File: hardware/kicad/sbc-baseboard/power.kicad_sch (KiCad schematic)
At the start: 85 parts, among them J17 Qwiic PD programming, J2 USB-C PD in, Q101 2N7002, Q102 2N7002, U101 STUSB4500QTR, U102 PCA9517A, U103 TPS54560BDDA, U104 TPS54560BDDA, U105 TPS62823DLC

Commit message: Reference-design review; pin numbers and real text widths in the layout gate
Review (docs/reference-design-review.md): every IC's surrounding parts
compared with its datasheet typical application or evaluation board.
Brought in line:
- TPS54560B compensation 16.9k / 4.7 nF / 47 pF (the 5 V / 400 kHz design
  example, same 141 uF ceramic output); the placeholders are gone.
- TPS62823 divider 453k / 100k with the 120 pF feed-forward capacitor the
  datasheet recommends.
- USB2517 VBUS_DET from the EVB: 100k / 100k with 1 uF (was 10k / 22k, 3.4 V
  at a 3.3 V pin).
- KSZ8081 MDIO pull-up 1.0k as the datasheet requires (was 4.7k).
- FT231X: 27 R in series and 47 pF on USBDM/USBDP, datasheet figure 6.1.
Deviations kept and documented: the bucks' EN gated by the PD controller
instead of a UVLO divider, the FT231X fed by a power switch instead of a
ferrite bead, translator OE tied to the target rail.

Layout gate: pin numbers are text boxes like any other, and all text widths
come from a per-glyph table fitted to the extents KiCad writes into its PDF
(check_pins.py); the generator's spacing uses the same table. That exposed
and fixed: reference/value overlaps on narrow symbols (now stacked), rail
names printed over each other (the lane end and hanging pull-up now carry
half the rail name), a port-switch value over its pin number, turned parts
with text on the pin side, lane stacks whose spread collapsed at the grid
snap, routes landing on connector pin stubs (J16, J601, J14, D202 moved),
the PD controller's I2C and gate routes that crossed half the sheet (now
labels), and the port /FAULT and I2C1 pull-ups, which as hanging resistors
staggered off the sheet and are now one column to one +3V3 symbol. The
port switch carries FAULT above OUT so the switched rail's parts hang below
the label; the VBUS row is drawn from the connector back to the switch.

All sheets: ERC 0, contacts 0, merges 0, layout 0 in every category.
Connectivity against 8579cd2 differs only in the value ch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
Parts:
- added C132: 120p, Capacitor_SMD:C_0603_1608Metric, symbol Device:C
- C115, C124: value 3n3 -> 4n7
- J17: value Qwiic PD programming -> Qwiic PD
- R117, R122: value 19.1k -> 16.9k
- R127: value 22.1k -> 100k
- R128: value 100k -> 453k
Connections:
- net +3V3: now also C132.1
- net PD_EN_GATE: now reaches D108.1 (K), Q101.1 (G), R107.2, U101.16 (VBUS_EN_SNK)
- net at R127.1, R128.2, U105.2 (FB): now also C132.2
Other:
- note added: "FB 51.1k/9.76k -> 5.0 V. COMP 16.9k / 4.7n / 47p and the B560C are the"
- note added: "datasheet's 5 V / 400 kHz design example (141 uF ceramic out, as here)."
- note removed: "FB 51.1k/9.76k -> 5.0 V. COMP values are placeholders (19.1k / 3.3n / 47p):"
- note removed: "run TI WEBENCH or the datasheet procedure before fab."

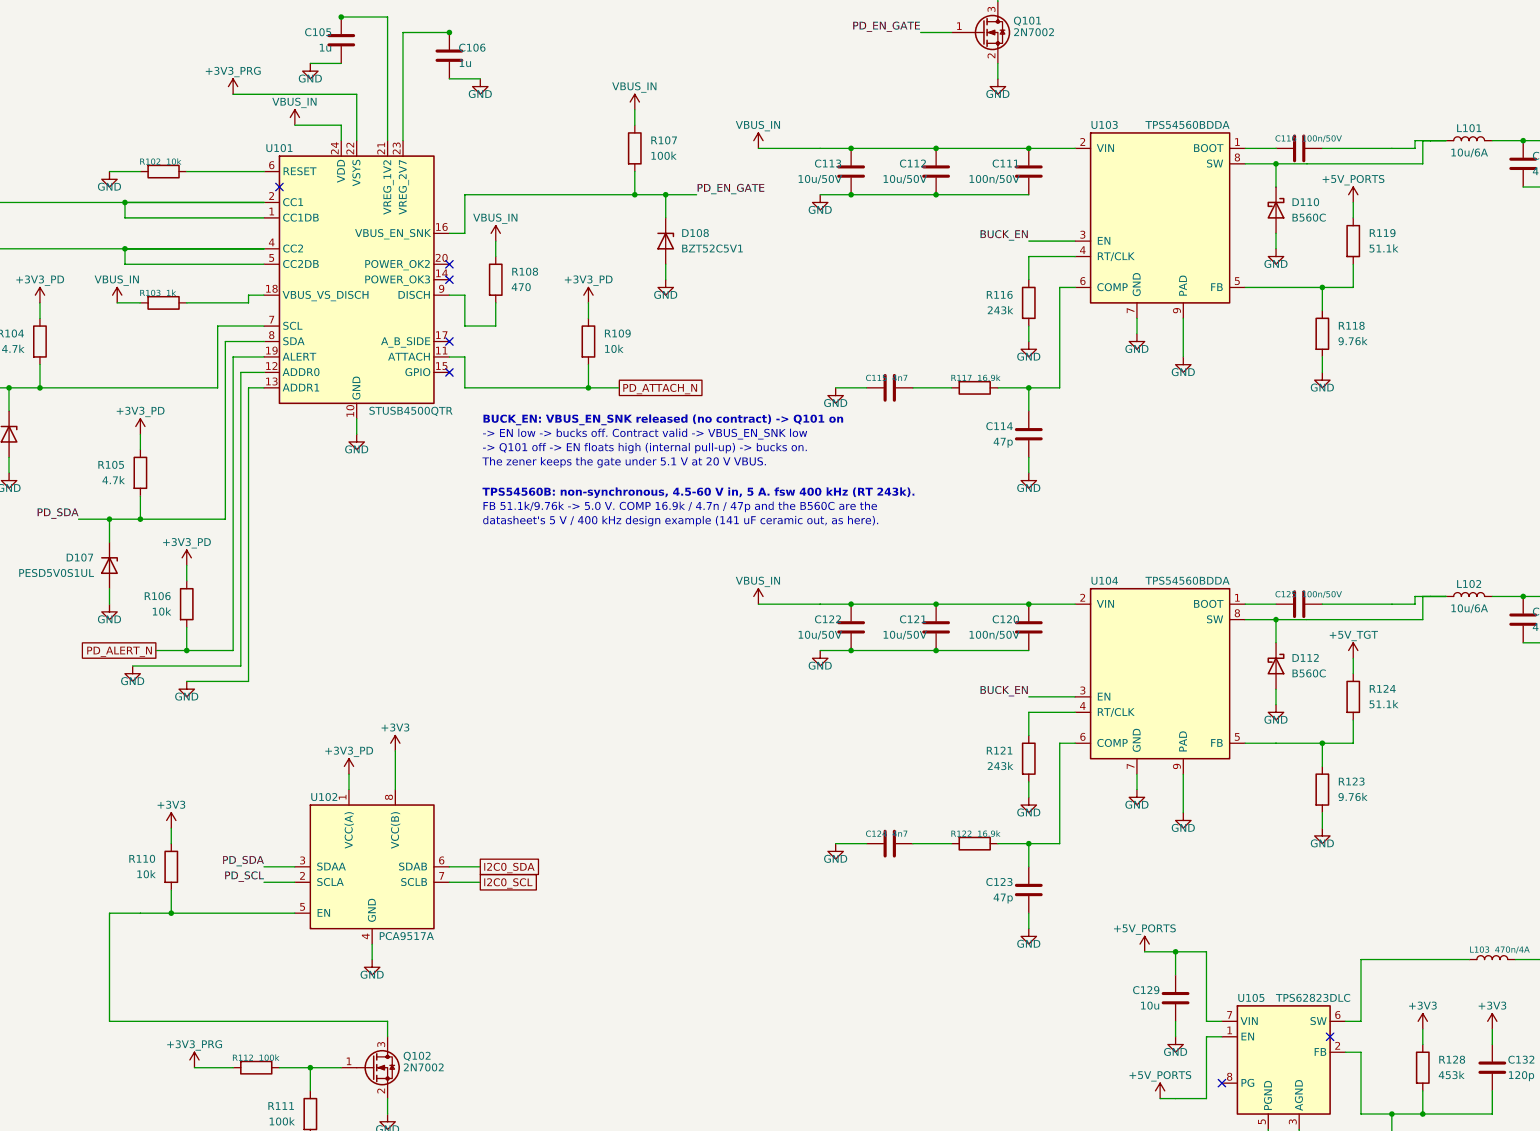
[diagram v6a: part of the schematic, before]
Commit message: House symbols from the ecad-libraries submodule
The project symbols move to calicopizzadelivery/ecad-libraries, added as a
submodule at hardware/kicad/libs and pinned to v0.1.1. The generator loads
them from the submodule's files (kisym.EXTRA_LIBS), so the embedded copies
match the library exactly; sym-lib-table and fp-lib-table are the fragments
the library ships, naming calico-ic and calico-electromechanical as
${KIPRJMOD}/../libs/... gen/parts.py and the project .kicad_sym are gone.

The symbols now follow the KiCad Library Conventions (every pin on the 100 mil
grid of the origin, 20 mil name offset), which moved a few pin rows; the port
blocks are re-aligned to the stacked USB-A's new rows. All sheets: ERC 0,
contacts 0, merges 0, layout 0; connectivity unchanged.

Co-Authored-By: Claude Fable 5.1 <noreply@anthropic.com>
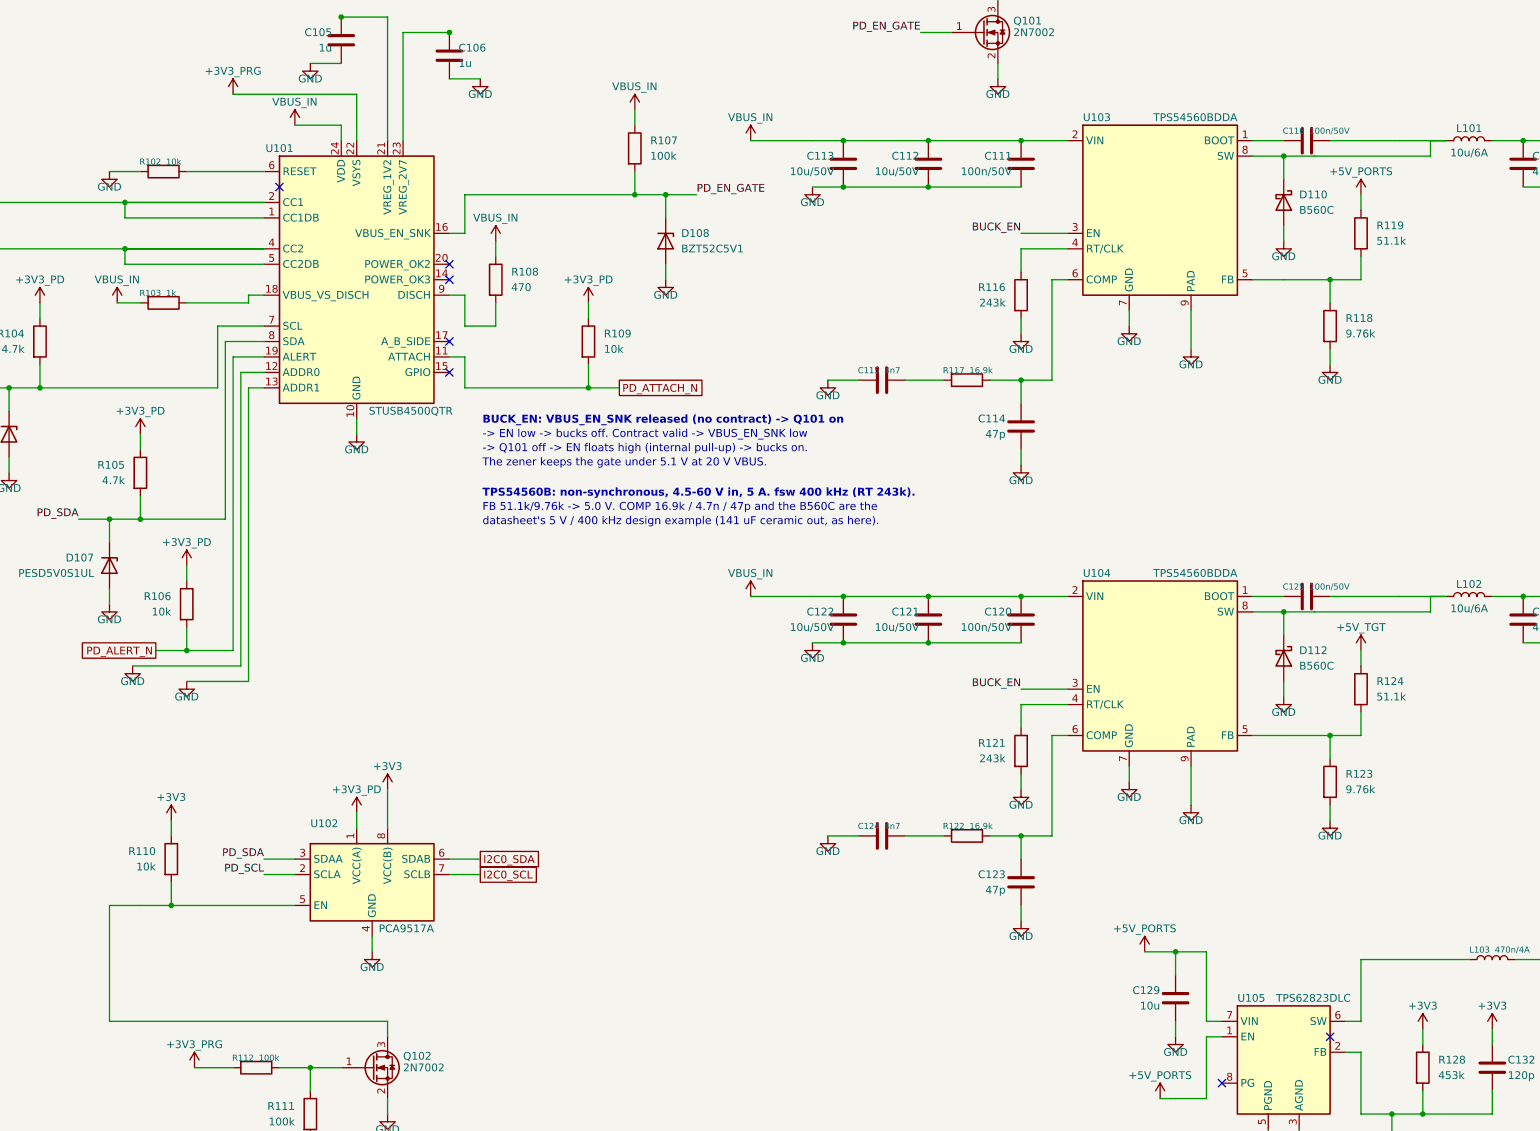
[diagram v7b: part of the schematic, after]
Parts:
- removed U102: PCA9517A, Package_SO:TSSOP-8_4.4x3mm_P0.65mm, symbol sbcbb:PCA9517A
- removed U103, U104: TPS54560BDDA, Package_SO:HSOP-8-1EP_3.9x4.9mm_P1.27mm_EP2.41x3.1mm, symbol sbcbb:TPS54560BDDA
- added U102: PCA9517A, Package_SO:TSSOP-8_4.4x3mm_P0.65mm, symbol calico-ic:PCA9517A
- added U103, U104: TPS54560BDDA, Package_SO:HSOP-8-1EP_3.9x4.9mm_P1.27mm_EP2.41x3.1mm, symbol calico-ic:TPS54560BDDA
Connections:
- net +3V3: now also U102.8 (VCC(B))
- net +3V3_PD: now also U102.1 (VCC(A))
- net BUCK_EN: now also U103.3 (EN), U104.3 (EN)
- net GND: now also U102.4 (GND), U103.7 (GND), U103.9 (PAD), U104.7 (GND), U104.9 (PAD)
- net I2C0_SCL: now also U102.7 (SCLB)
- net I2C0_SDA: now also U102.6 (SDAB)
- net PD_SCL: now also U102.2 (SCLA)
- net PD_SDA: now also U102.3 (SDAA)
- net VBUS_IN: now also U103.2 (VIN), U104.2 (VIN)
- net at R116.1: now also U103.4 (RT/CLK)
- net at Q102.3 (D), R110.2: now also U102.5 (EN)
- net at R118.1, R119.2: now also U103.5 (FB)
- net at R123.1, R124.2: now also U104.5 (FB)
- net at C125.1: now also U104.1 (BOOT)
- net at R121.1: now also U104.4 (RT/CLK)
- net at C123.1, R122.1: now also U104.6 (COMP)
- net at C125.2, D112.1 (K), L102.1: now also U104.8 (SW)
- net at C116.2, D110.1 (K), L101.1: now also U103.8 (SW)
- net at C116.1: now also U103.1 (BOOT)
- net at C114.1, R117.1: now also U103.6 (COMP)
